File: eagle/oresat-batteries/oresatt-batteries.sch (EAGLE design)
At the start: 6 parts, among them U1 TCAN330

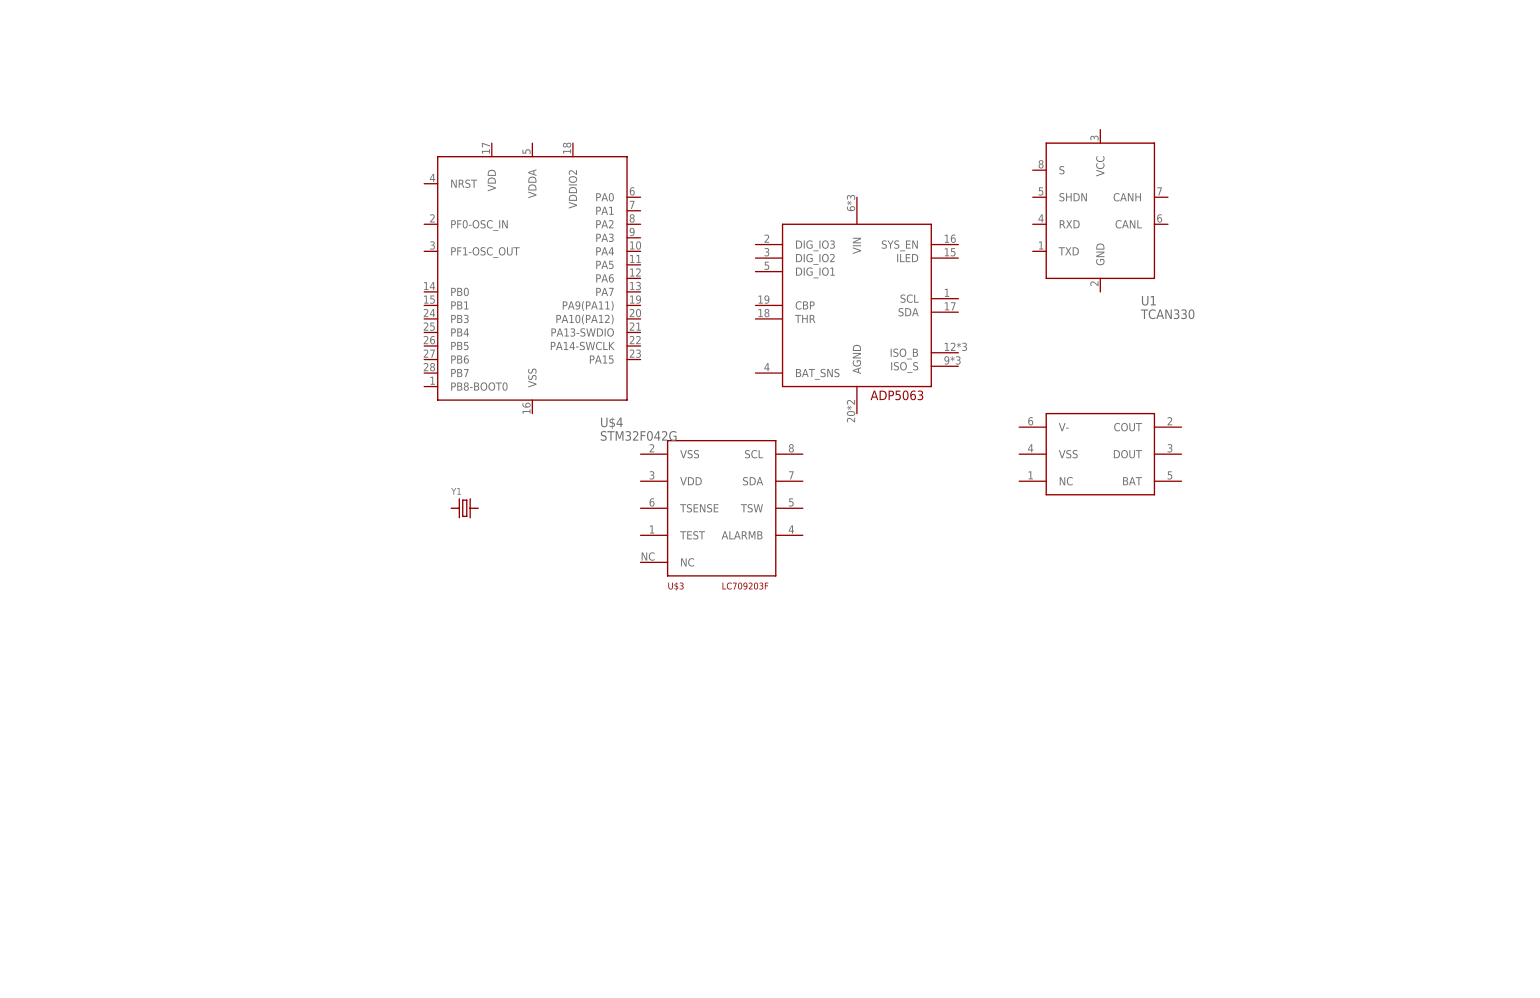
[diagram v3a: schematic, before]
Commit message: Added 40 pin for real this time.
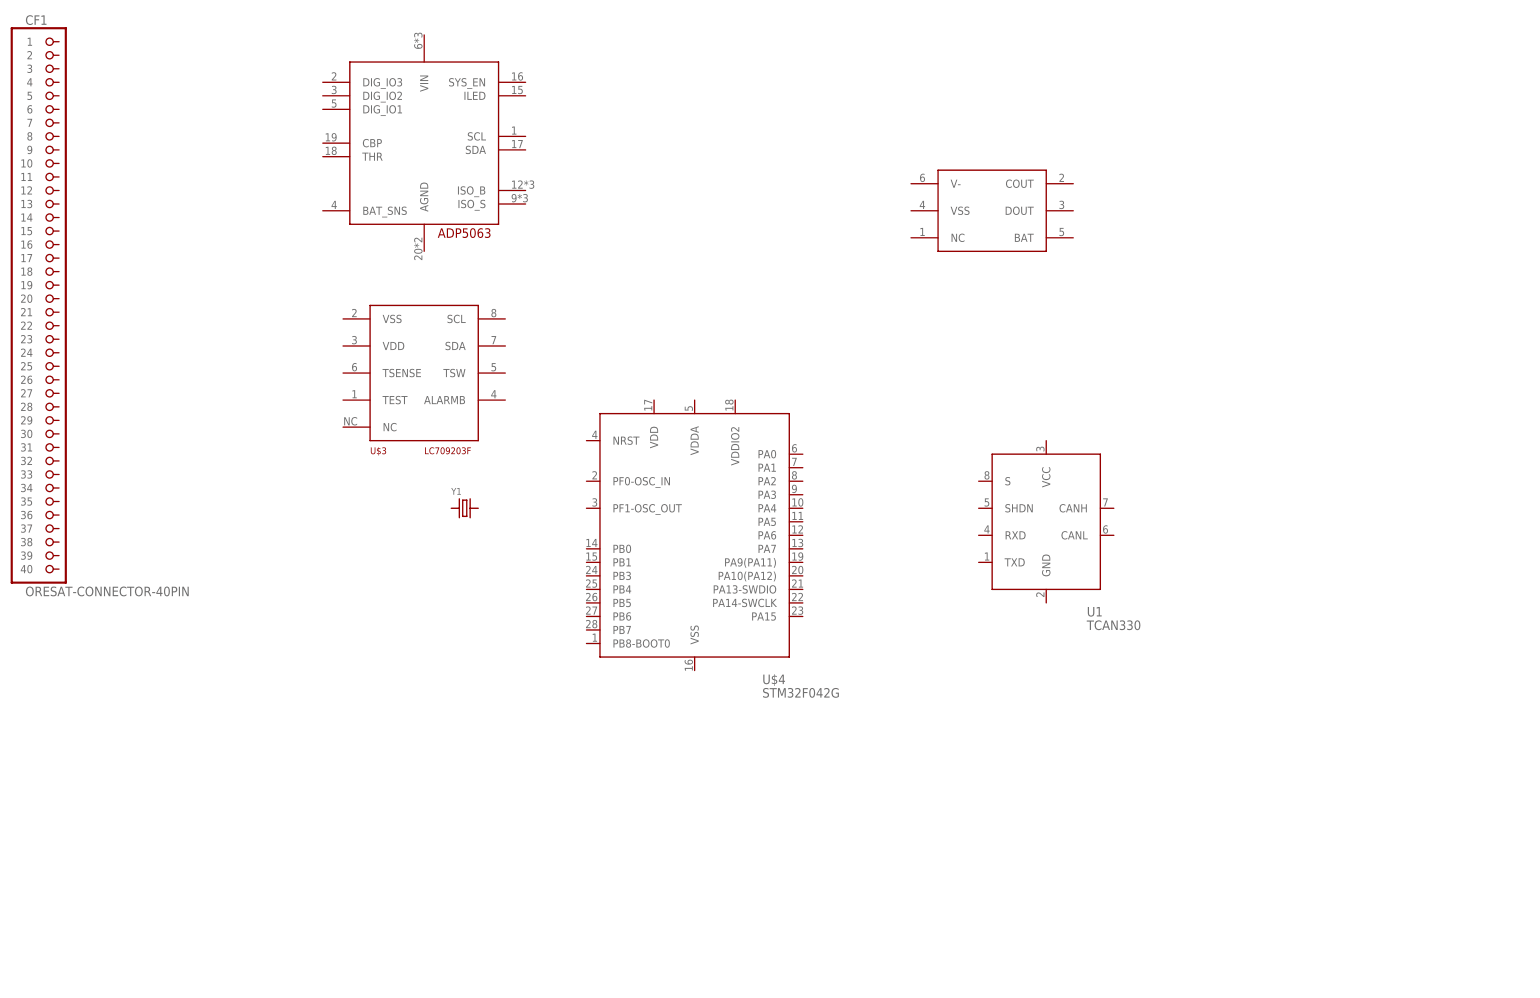
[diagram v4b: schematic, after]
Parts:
- added CF1: ORESAT-CONNECTOR-40PIN, low-gain-radio:ORESAT-CONNECTOR-40PIN
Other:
- moved on the sheet: U$3, U$4, U1
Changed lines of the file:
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@@
 <part name="U1" library="oresat-batteries" deviceset="TCAN330" device=""/>
 <part name="Y1" library="low-gain-radio" deviceset="CRYSTAL" device="2.5X2.0MM"/>
+<part name="CF1" library="low-gain-radio" deviceset="ORESAT-CONNECTOR-40PIN" device=""/>
 </parts>
 <sheets>
@@
 </plain>
 <instances>
-<instance part="U$1" gate="G$1" x="0" y="0"/>
-<instance part="U$2" gate="G$1" x="45.72" y="-27.94"/>
-<instance part="U$3" gate="G$1" x="-25.4" y="-38.1"/>
-<instance part="U$4" gate="G$1" x="-60.96" y="5.08"/>
-<instance part="U1" gate="G$1" x="45.72" y="17.78"/>
+<instance part="U$1" gate="G$1" x="-81.28" y="30.48"/>
+<instance part="U$2" gate="G$1" x="25.4" y="17.78"/>
+<instance part="U$3" gate="G$1" x="-81.28" y="-12.7"/>
+<instance part="U$4" gate="G$1" x="-30.48" y="-43.18"/>
+<instance part="U1" gate="G$1" x="35.56" y="-40.64"/>
 <instance part="Y1" gate="G$1" x="-73.66" y="-38.1"/>
+<instance part="CF1" gate="G$1" x="-149.86" y="0"/>
 </instances>
 <busses>

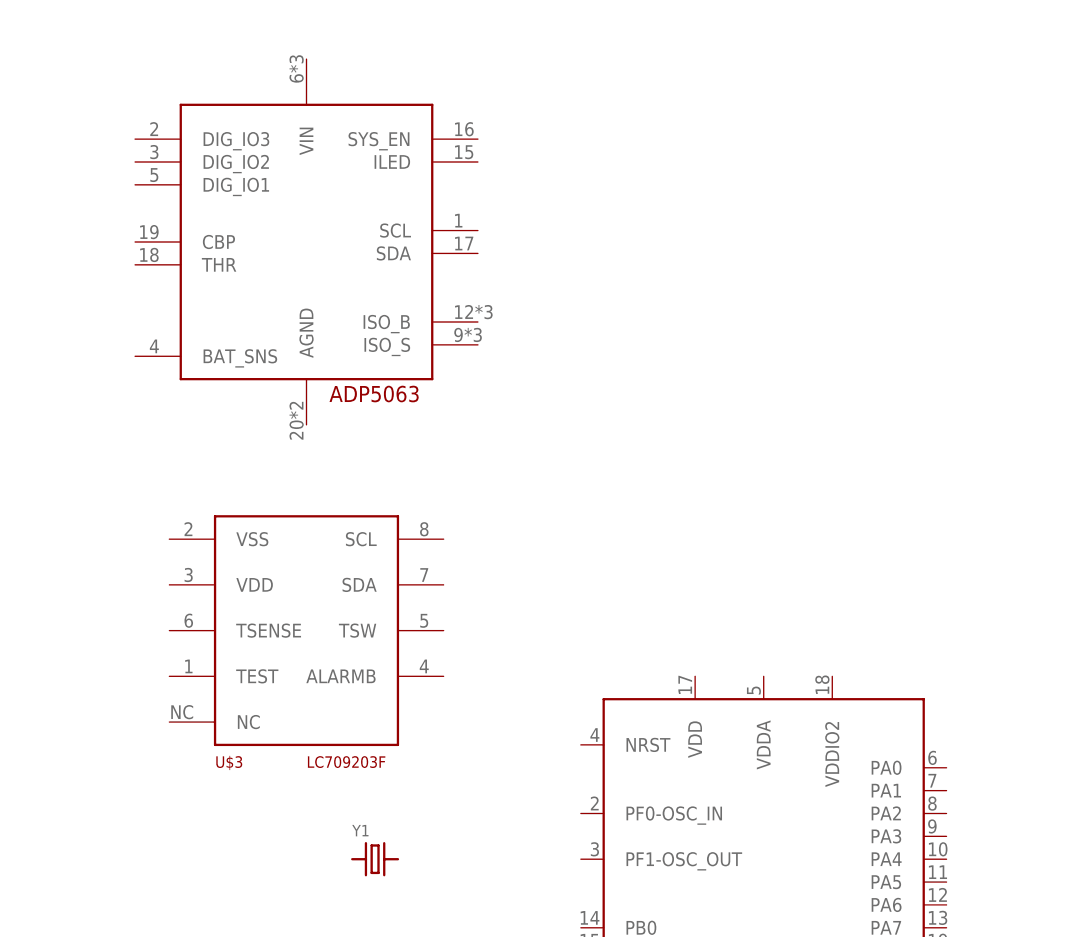
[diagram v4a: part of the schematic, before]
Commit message: Swapped fuel gauge for ti BQ27500
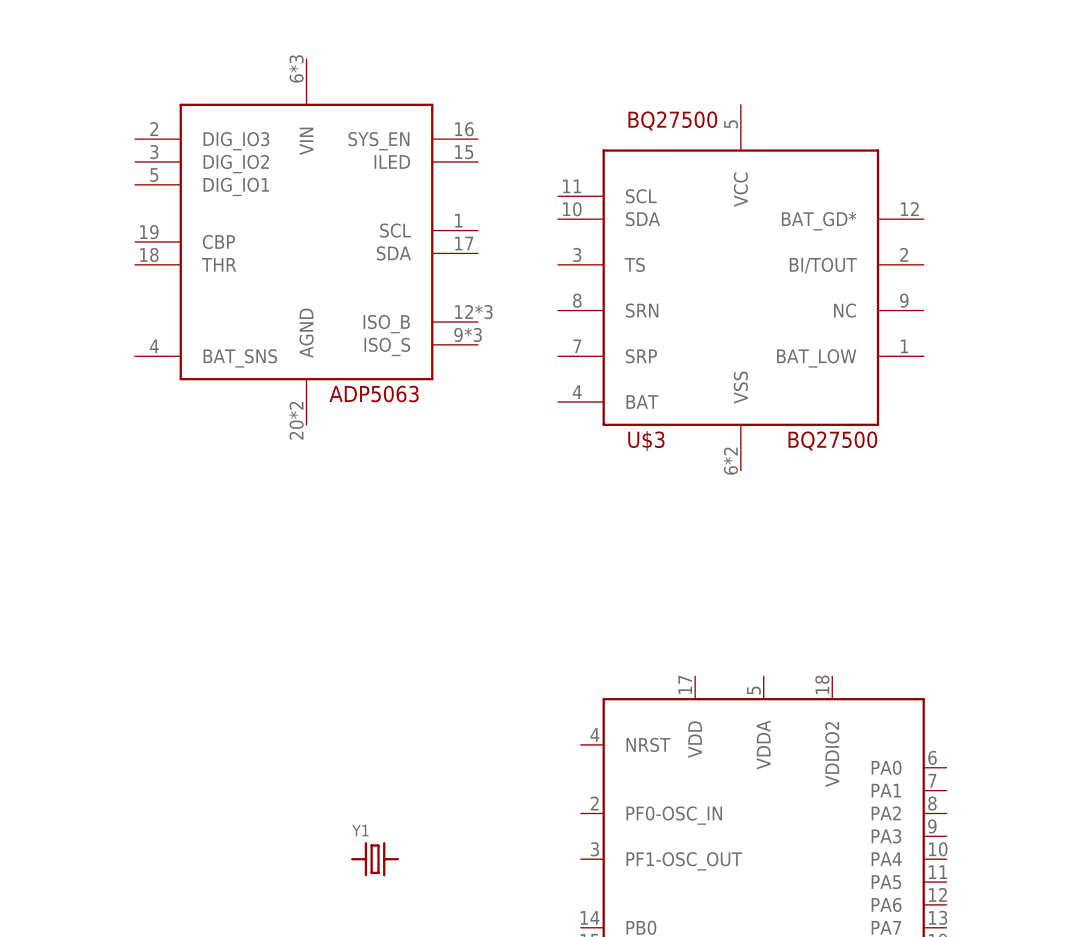
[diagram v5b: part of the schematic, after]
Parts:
- U$3: value LC709203F -> BQ27500; device oresat-batteries:LC709203F -> oresat-batteries:BQ27500
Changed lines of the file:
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@@
 </layers>
 <schematic xreflabel="%F%N/%S.%C%R" xrefpart="/%S.%C%R">
+<description>Oresat
+Battery Management Board v0
+Andrew Greenberg
+Austin Joseph
+Haneef Mubarak</description>
 <attributes>
 </attributes>
@@
 <part name="U$1" library="oresat-batteries" deviceset="ADP5063" device=""/>
 <part name="U$2" library="oresat-batteries" deviceset="BQ2970" device=""/>
-<part name="U$3" library="oresat-batteries" deviceset="LC709203F" device=""/>
 <part name="U$4" library="oresat-batteries" deviceset="STM32F042G" device=""/>
 <part name="U1" library="oresat-batteries" deviceset="TCAN330" device=""/>
 <part name="Y1" library="low-gain-radio" deviceset="CRYSTAL" device="2.5X2.0MM"/>
 <part name="CF1" library="low-gain-radio" deviceset="ORESAT-CONNECTOR-40PIN" device=""/>
+<part name="U$3" library="oresat-batteries" deviceset="BQ27500" device=""/>
 </parts>
 <sheets>
@@
 <instance part="U$1" gate="G$1" x="-81.28" y="30.48"/>
 <instance part="U$2" gate="G$1" x="25.4" y="17.78"/>
-<instance part="U$3" gate="G$1" x="-81.28" y="-12.7"/>
 <instance part="U$4" gate="G$1" x="-30.48" y="-43.18"/>
 <instance part="U1" gate="G$1" x="35.56" y="-40.64"/>
 <instance part="Y1" gate="G$1" x="-73.66" y="-38.1"/>
 <instance part="CF1" gate="G$1" x="-149.86" y="0"/>
+<instance part="U$3" gate="G$1" x="-33.02" y="25.4"/>
 </instances>
 <busses>

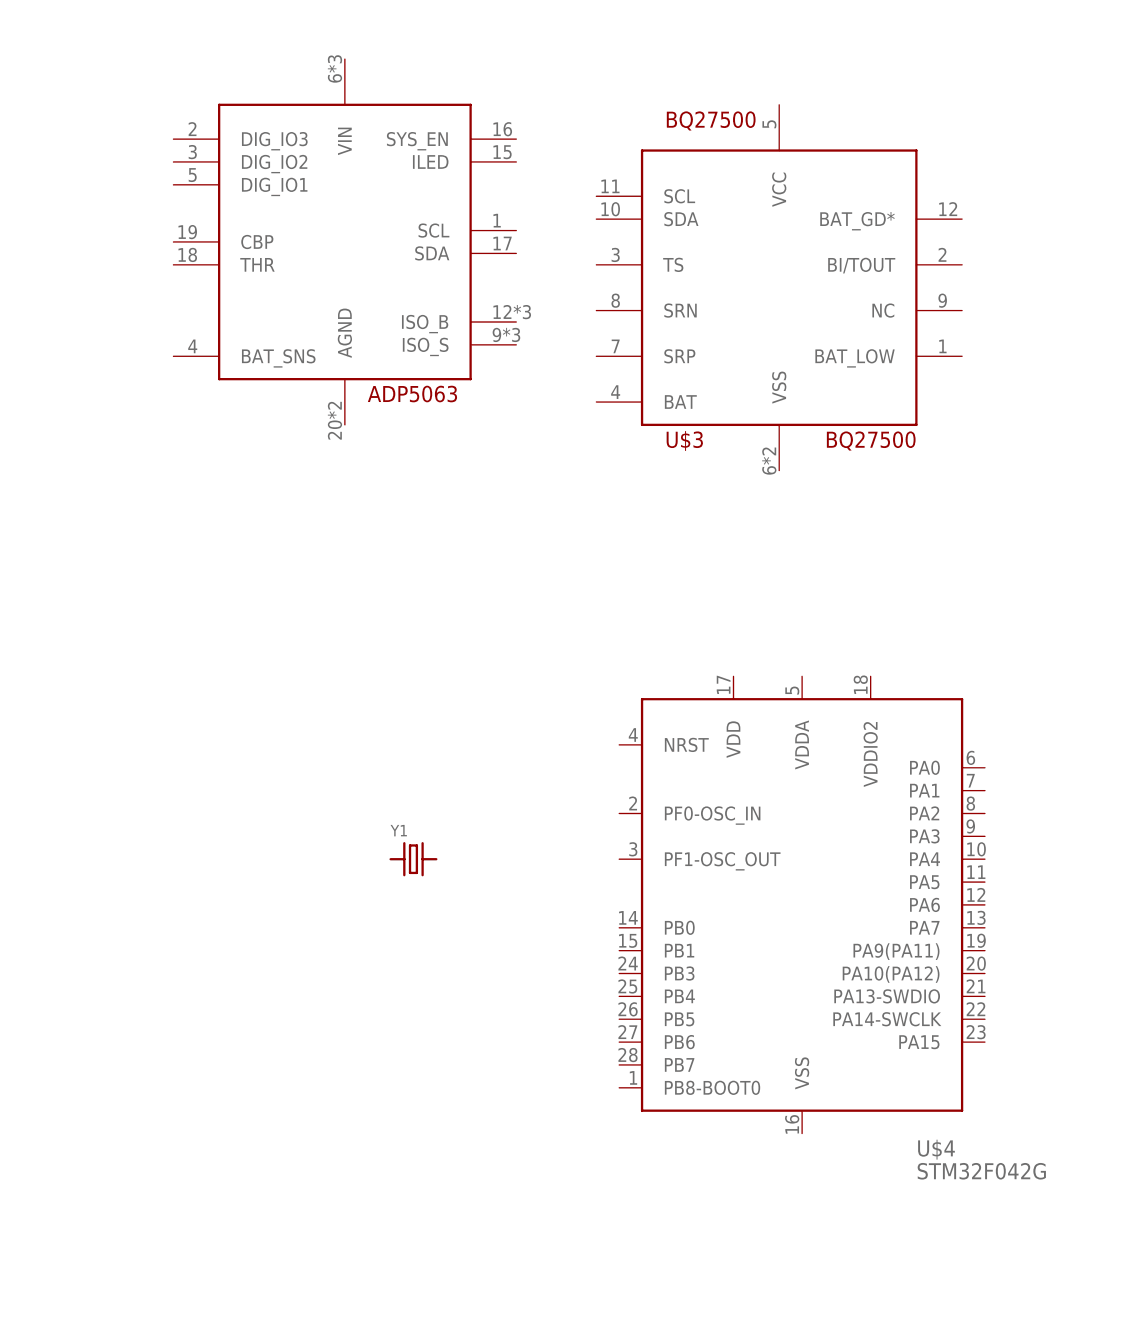
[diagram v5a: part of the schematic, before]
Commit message: Replaced BQ27500 with STC300lST
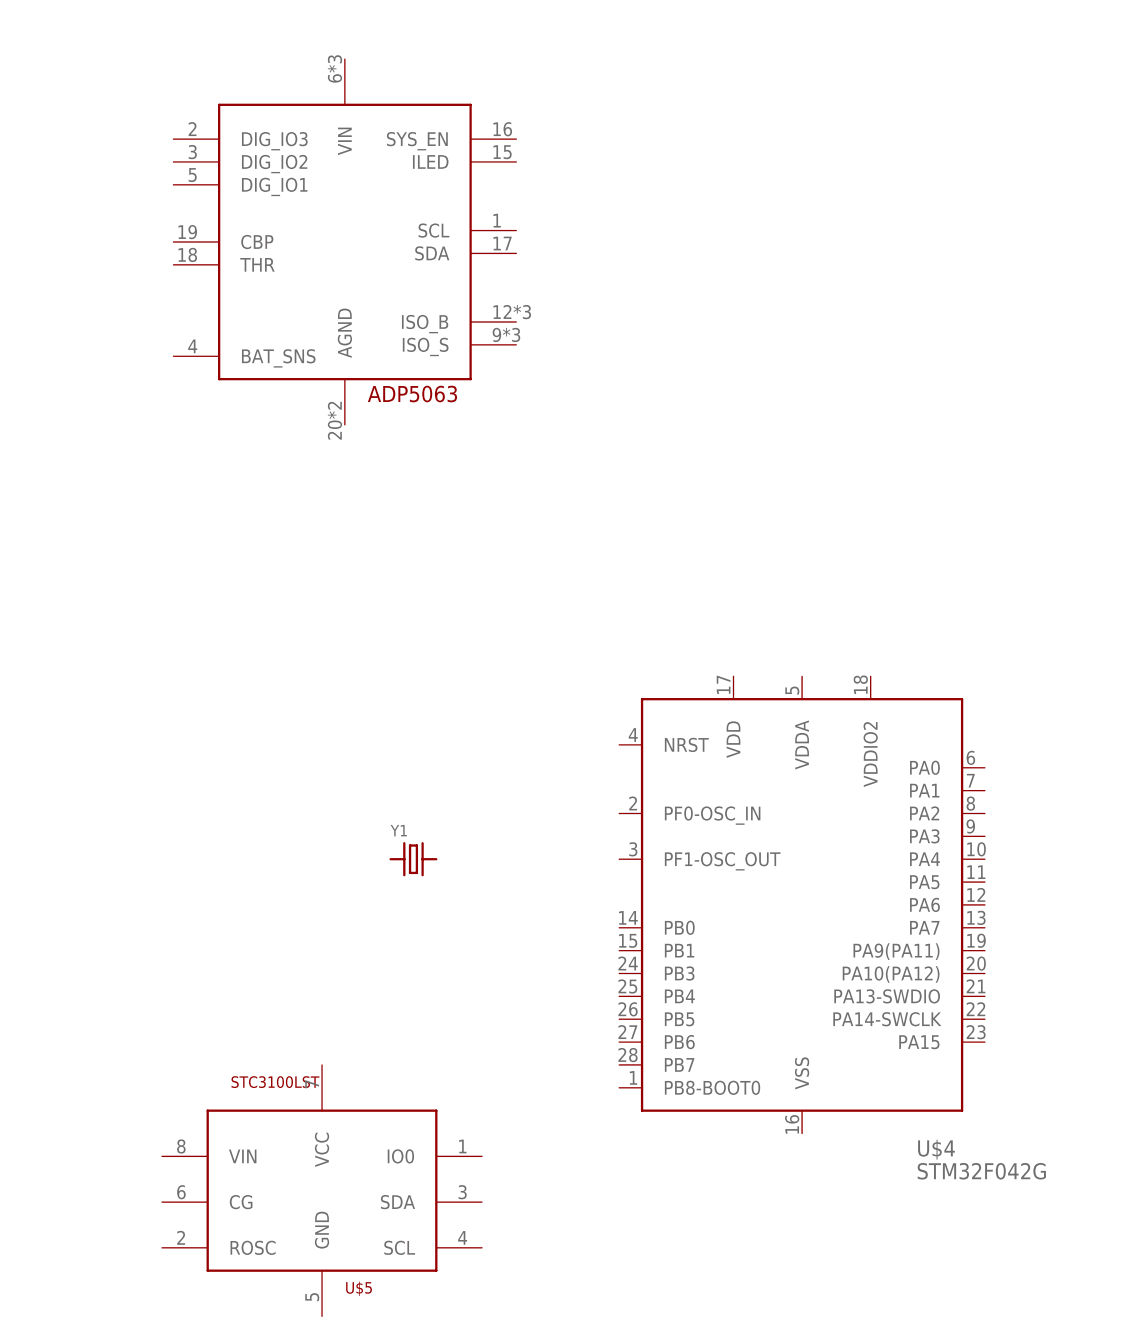
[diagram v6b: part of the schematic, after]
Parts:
- removed U$3: BQ27500, oresat-batteries:BQ27500
- added U$5: STC3100LST, oresat-batteries:STC3100LST
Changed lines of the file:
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@@
 <part name="Y1" library="low-gain-radio" deviceset="CRYSTAL" device="2.5X2.0MM"/>
 <part name="CF1" library="low-gain-radio" deviceset="ORESAT-CONNECTOR-40PIN" device=""/>
-<part name="U$3" library="oresat-batteries" deviceset="BQ27500" device=""/>
+<part name="U$5" library="oresat-batteries" deviceset="STC3100LST" device=""/>
 </parts>
 <sheets>
@@
 <instance part="Y1" gate="G$1" x="-73.66" y="-38.1"/>
 <instance part="CF1" gate="G$1" x="-149.86" y="0"/>
-<instance part="U$3" gate="G$1" x="-33.02" y="25.4"/>
+<instance part="U$5" gate="G$1" x="-83.82" y="-73.66"/>
 </instances>
 <busses>
